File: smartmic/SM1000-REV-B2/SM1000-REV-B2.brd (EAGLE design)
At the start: 65 x 90 mm, 176 parts, among them CN1 HDR100-3, CN10 MJ-3523-SMT, CN11 HDR100-3, CN12 DF11-16DS, CN2 MOLEX-MINI-B-SMT, CN3 RASM712PX, CN4 RJ-45, CN5 MJ-3523-SMT, CN6 MJ-3523-SMT, CN7 MJ-3523-SMT, CN8 MJ-3523-SMT, CN9 MJ-3523-SMT, J1 JMP-2PIN, J2 JMP-2PIN, J3 JMP-2PIN, J4 JMP-2PIN, J5 JMP-2PIN, J7 JMP-2PIN, P1 TPAD50, P10 TPAD50, P11 TPAD50, P12 TPAD50, P13 TPAD50, P14 TPAD50, P15 TPAD50, P16 TPAD50, P17 TPAD50, P18 TPAD50, P19 TPAD50, P2 TPAD50, P20 TPAD50, P3 TPAD50, P4 TPAD50, P5 TPAD50, P6 TPAD50, P7 TPAD50, P8 TPAD50, P9 TPAD50, SW1 SW-BOURNS-7914S, SW2 SW-BOURNS-7914S, SW3 DPDT, SW4 SW-BOURNS-7914S, T1 SM-LP-5001, T2 SM-LP-5001, U1 STM32F405, U2 LD3985M33R, U3 STMPS2141, U4 EMIF02-USB03F2, U5 TPS54329E, U6 LMV341, U7 LMV341, U8 LM386M-1, U9 LMV341

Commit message: Updates indicated in change log - RGB
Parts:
- moved LED5 0.50 mm to (21.2, 44.0)
- moved LED8 0.50 mm to (2.50, 48.5)
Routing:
- net +3.3V: track 19.8 -> 20.8 mm
- net N$19: track 2.52 -> 3.27 mm
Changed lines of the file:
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@@
 <layer number="17" name="Pads" color="2" fill="1" visible="yes" active="yes"/>
 <layer number="18" name="Vias" color="2" fill="1" visible="yes" active="yes"/>
-<layer number="19" name="Unrouted" color="6" fill="1" visible="no" active="yes"/>
+<layer number="19" name="Unrouted" color="6" fill="1" visible="yes" active="yes"/>
 <layer number="20" name="Dimension" color="15" fill="1" visible="yes" active="yes"/>
-<layer number="21" name="tPlace" color="7" fill="1" visible="no" active="yes"/>
+<layer number="21" name="tPlace" color="7" fill="1" visible="yes" active="yes"/>
 <layer number="22" name="bPlace" color="7" fill="1" visible="no" active="yes"/>
 <layer number="23" name="tOrigins" color="15" fill="1" visible="yes" active="yes"/>
 <layer number="24" name="bOrigins" color="15" fill="1" visible="no" active="yes"/>
-<layer number="25" name="tNames" color="7" fill="1" visible="no" active="yes"/>
+<layer number="25" name="tNames" color="7" fill="1" visible="yes" active="yes"/>
 <layer number="26" name="bNames" color="7" fill="1" visible="no" active="yes"/>
 <layer number="27" name="tValues" color="7" fill="1" visible="no" active="yes"/>
@@
 <layer number="200" name="200bmp" color="1" fill="10" visible="no" active="no"/>
 <layer number="201" name="Construction" color="7" fill="1" visible="no" active="yes"/>
-<layer number="202" name="TDIM" color="7" fill="1" visible="yes" active="yes"/>
+<layer number="202" name="TDIM" color="7" fill="1" visible="no" active="yes"/>
 <layer number="203" name="BDIM" color="7" fill="1" visible="no" active="yes"/>
 <layer number="204" name="BRD-DIM" color="7" fill="1" visible="no" active="yes"/>
@@
 <attribute name="VALUE" x="5.4625" y="49.25" size="1" layer="27" font="vector" ratio="10" rot="R270"/>
 </element>
-<element name="LED5" library="_Coherix" package="LED-LTST" value="LED-RED,V" x="21.25" y="44.5" locked="yes" smashed="yes" rot="R270">
-<attribute name="NAME" x="21.8" y="42.05" size="0.8128" layer="25"/>
+<element name="LED5" library="_Coherix" package="LED-LTST" value="LED-RED,V" x="21.25" y="44" locked="yes" smashed="yes" rot="R270">
+<attribute name="NAME" x="22.2" y="42.05" size="0.8128" layer="25"/>
 </element>
 <element name="R17" library="AA-ipc-7351-resistor" package="RESC1608X55N" value="1K,1%" x="18.75" y="44.5" locked="yes" smashed="yes" rot="R90">
@@
 <attribute name="NAME" x="4" y="49.7" size="0.8128" layer="25"/>
 </element>
-<element name="LED8" library="_Coherix" package="LED-LTST" value="LED-RED,RA" x="2.5" y="48" locked="yes" smashed="yes" rot="R270">
-<attribute name="NAME" x="1.2" y="45.5" size="0.8128" layer="25"/>
+<element name="LED8" library="_Coherix" package="LED-LTST" value="LED-RED,RA" x="2.5" y="48.5" locked="yes" smashed="yes" rot="R270">
+<attribute name="NAME" x="0.8" y="45.4" size="0.8128" layer="25"/>
 </element>
 <element name="CN9" library="_RoweTel" package="MJ-3523-SMT" value="MJ-3523-SMT" x="43" y="8" locked="yes" smashed="yes" rot="MR270">
@@
 <wire x1="18.75" y1="46.95" x2="21.25" y2="46.95" width="0.4" layer="1"/>
 <polygon width="0.2" layer="1" isolate="0.3">
-<vertex x="3.5" y="50"/>
-<vertex x="1" y="50"/>
+<vertex x="3.5" y="51"/>
+<vertex x="1" y="51"/>
 <vertex x="1" y="46"/>
 <vertex x="6.5" y="46"/>
@@
 <wire x1="23.75" y1="48.55" x2="21.25" y2="48.55" width="0.4" layer="1"/>
 <wire x1="18.75" y1="48.55" x2="21.25" y2="48.55" width="0.4" layer="1"/>
-<wire x1="18.75" y1="45.3" x2="19.7" y2="45.3" width="0.2" layer="1"/>
-<wire x1="19.7" y1="45.3" x2="20.5" y2="44.5" width="0.2" layer="1"/>
-<wire x1="20.5" y1="44.5" x2="22" y2="44.5" width="0.2" layer="1"/>
-<wire x1="22" y1="44.5" x2="22.5" y2="45" width="0.2" layer="1"/>
+<wire x1="18.75" y1="45.3" x2="19.2" y2="45.3" width="0.2" layer="1"/>
 <wire x1="22.5" y1="45" x2="22.5" y2="47" width="0.2" layer="1"/>
 <wire x1="22.5" y1="47" x2="23.02" y2="47.52" width="0.2" layer="1"/>
@@
 <wire x1="15" y1="46.5" x2="17.05" y2="48.55" width="0.4" layer="1"/>
 <wire x1="17.05" y1="48.55" x2="18.75" y2="48.55" width="0.4" layer="1"/>
+<wire x1="19.2" y1="45.3" x2="19.5" y2="45.3" width="0.2" layer="1"/>
+<wire x1="19.5" y1="45.3" x2="19.7" y2="45.3" width="0.2" layer="1"/>
+<wire x1="19.7" y1="45.3" x2="20" y2="45" width="0.2" layer="1"/>
+<wire x1="20" y1="45" x2="20" y2="44.5" width="0.2" layer="1"/>
+<wire x1="20" y1="44.5" x2="20.5" y2="44" width="0.2" layer="1"/>
+<wire x1="20.5" y1="44" x2="22" y2="44" width="0.2" layer="1"/>
+<wire x1="22" y1="44" x2="22.5" y2="44.5" width="0.2" layer="1"/>
+<wire x1="22.5" y1="44.5" x2="22.5" y2="45" width="0.2" layer="1"/>
 </signal>
 <signal name="+5V">
@@
 <contactref element="LED5" pad="A"/>
 <contactref element="R17" pad="1"/>
-<wire x1="18.75" y1="43.7" x2="21.2" y2="43.7" width="0.4" layer="1"/>
-<wire x1="21.2" y1="43.7" x2="21.25" y2="43.75" width="0.4" layer="1"/>
+<wire x1="18.75" y1="43.7" x2="18.75" y2="43.05" width="0.2" layer="1"/>
+<wire x1="18.75" y1="43.05" x2="19" y2="42.8" width="0.2" layer="1"/>
+<wire x1="19" y1="42.8" x2="19.05" y2="42.75" width="0.2" layer="1"/>
+<wire x1="19.05" y1="42.75" x2="21.25" y2="42.75" width="0.2" layer="1"/>
 </signal>
 <signal name="N$16">

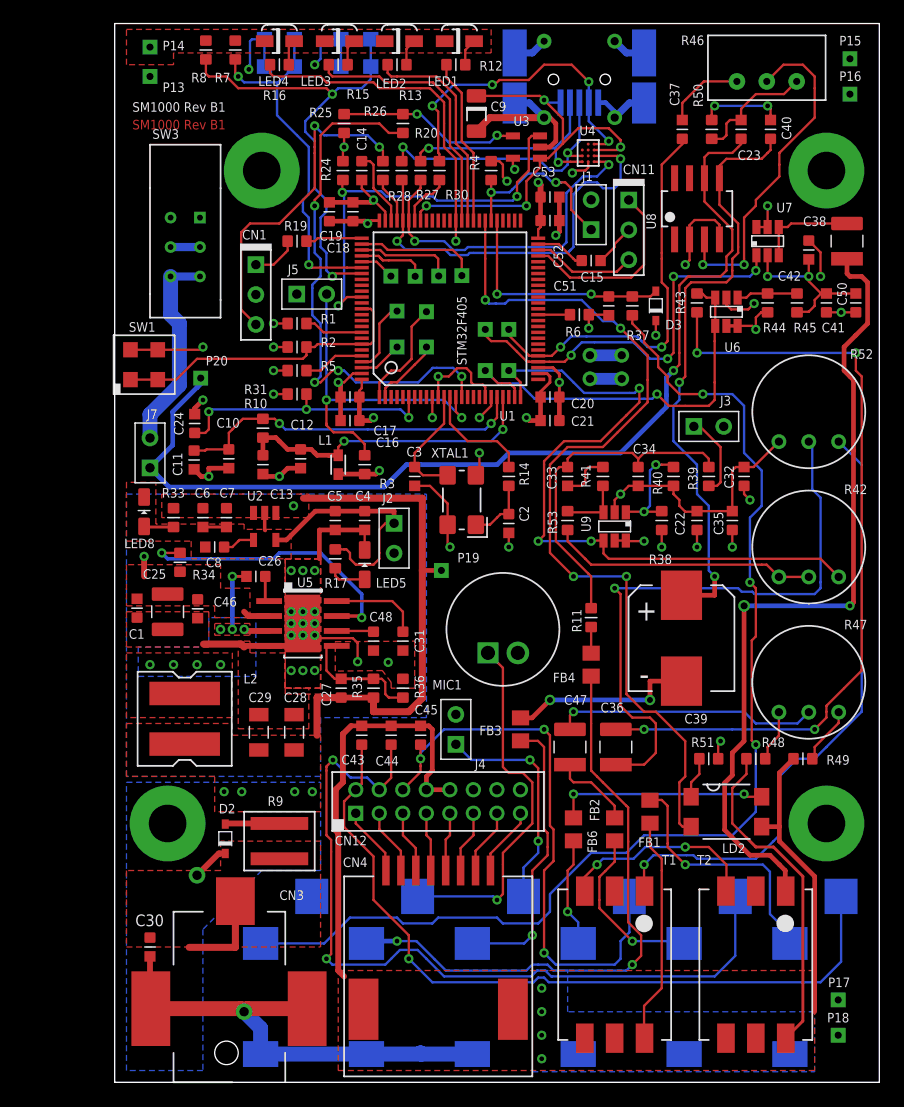
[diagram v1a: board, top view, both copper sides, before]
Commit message: 
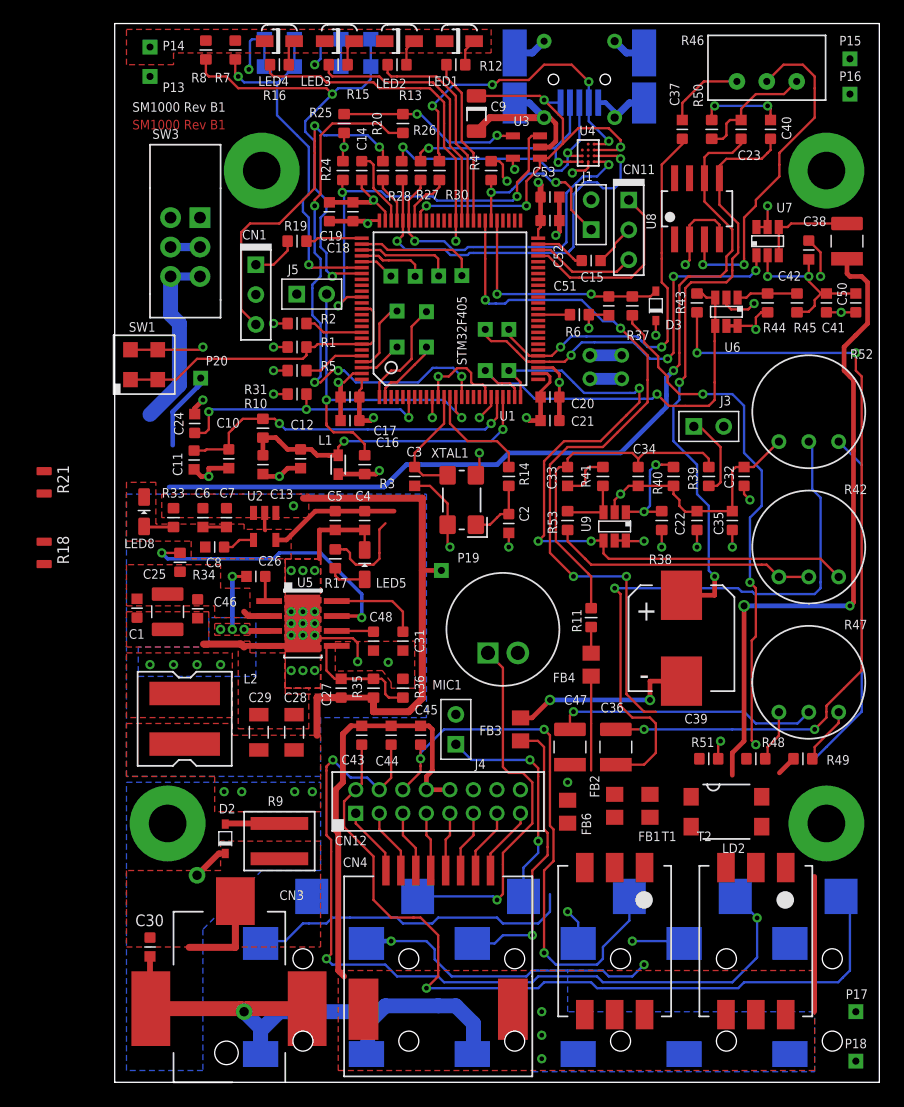
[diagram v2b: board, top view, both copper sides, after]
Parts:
- removed J2, J7: JMP-2PIN, _Coherix:JMPR-2PIN
- removed SH2, SH6: SHUNT,0.1IN, _Coherix:NOPACKAGE
- added R18, R21: 0 Ohm, _RoweTel:RR0805
- moved P18 2.66 mm to (63.0, 1.80)
- moved FB2 2.00 mm to (42.5, 23.5)
- moved T1 2.00 mm to (42.5, 12.0)
- moved T2 2.00 mm to (54.5, 12.0)
- moved P17 1.80 mm to (63.0, 6.00)
- moved FB6 1.58 mm to (38.5, 23.0)
- moved FB1 0.50 mm to (45.5, 23.5)
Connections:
- net +3.3V: now also R18.1; no longer J2.1
- net +VIN: now also R21.2; no longer J7.1
- net N$70: now also R21.1; no longer J7.2
- net VDD: now also R18.2; no longer J2.2
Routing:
- net VDD: track 89.5 -> 148.4 mm
- net N$78: track 28.2 -> 0.00 mm
- net N$85: track 98.7 -> 72.7 mm
- net N$63: track 53.1 -> 29.4 mm, vias 1 -> 0
- net N$64: track 21.6 -> 0.00 mm, vias 1 -> 0
- net N$33: track 19.3 -> 0.00 mm
- net N$74: track 18.1 -> 0.00 mm, vias 2 -> 1
- net N$76: track 50.9 -> 34.3 mm
- net +VIN: track 100.8 -> 84.2 mm, vias 2 -> 1
- net N$65: track 69.2 -> 55.9 mm
- net !CPPT!: track 77.0 -> 65.2 mm
- net RF: track 61.2 -> 49.7 mm, vias 4 -> 3
- net N$72: track 14.7 -> 4.48 mm
- net N$79: track 6.98 -> 0.00 mm
- net N$73: track 9.30 -> 3.07 mm
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
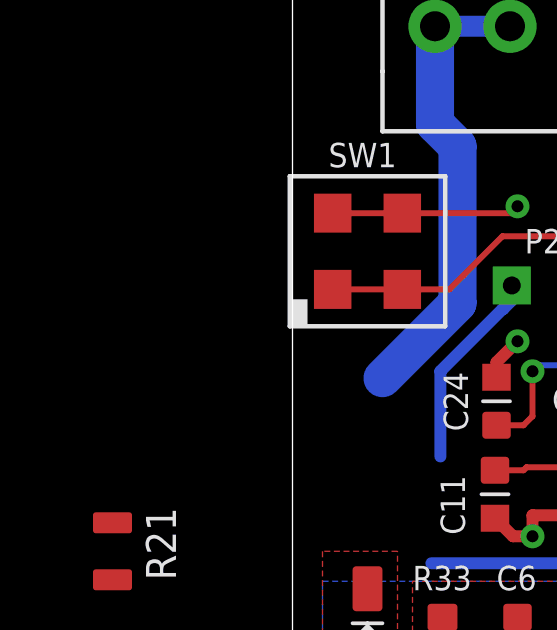
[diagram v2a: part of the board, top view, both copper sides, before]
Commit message: Items 1-5,7-12,14-20 have been implemented in schematic . Items 6 & 13 need discussion to resolve. PCB has been updated to reflect changes, but routing of changes has not been completed. Layout will be updated as time pemits. RGB - 07/17/2014
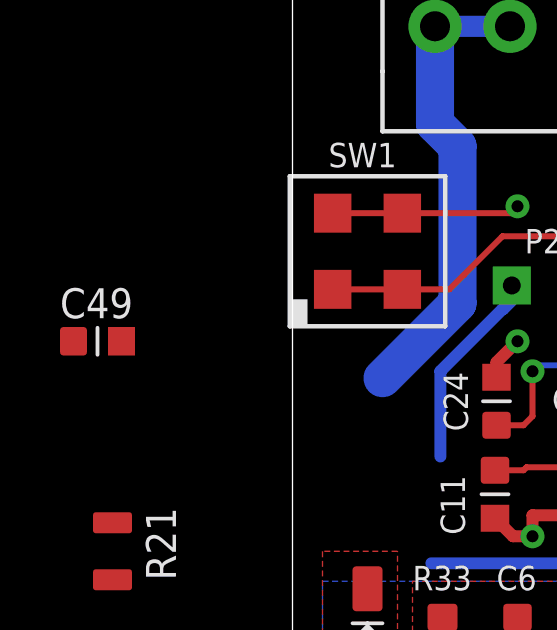
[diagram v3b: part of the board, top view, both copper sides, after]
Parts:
- added C49: 100nF,16V, AA-ipc-7351-capacitor:CAPC1608X92N
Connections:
- net GND: now also C49.2
- net NRST: now also C49.1
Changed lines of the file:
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@@
 <grid distance="0.5" unitdist="mm" unit="mm" style="dots" multiple="1" display="yes" altdistance="0.1" altunitdist="mm" altunit="mm"/>
 <layers>
-<layer number="1" name="Top" color="4" fill="1" visible="no" active="yes"/>
-<layer number="2" name="GND" color="3" fill="1" visible="no" active="yes"/>
+<layer number="1" name="Top" color="4" fill="1" visible="yes" active="yes"/>
+<layer number="2" name="GND" color="3" fill="1" visible="yes" active="yes"/>
 <layer number="3" name="Route3" color="4" fill="3" visible="no" active="no"/>
 <layer number="4" name="Route4" color="1" fill="4" visible="no" active="no"/>
@@
 <layer number="19" name="Unrouted" color="6" fill="1" visible="yes" active="yes"/>
 <layer number="20" name="Dimension" color="15" fill="1" visible="yes" active="yes"/>
-<layer number="21" name="tPlace" color="7" fill="1" visible="no" active="yes"/>
-<layer number="22" name="bPlace" color="7" fill="1" visible="yes" active="yes"/>
-<layer number="23" name="tOrigins" color="15" fill="1" visible="no" active="yes"/>
-<layer number="24" name="bOrigins" color="15" fill="1" visible="yes" active="yes"/>
-<layer number="25" name="tNames" color="7" fill="1" visible="no" active="yes"/>
-<layer number="26" name="bNames" color="7" fill="1" visible="yes" active="yes"/>
+<layer number="21" name="tPlace" color="7" fill="1" visible="yes" active="yes"/>
+<layer number="22" name="bPlace" color="7" fill="1" visible="no" active="yes"/>
+<layer number="23" name="tOrigins" color="15" fill="1" visible="yes" active="yes"/>
+<layer number="24" name="bOrigins" color="15" fill="1" visible="no" active="yes"/>
+<layer number="25" name="tNames" color="7" fill="1" visible="yes" active="yes"/>
+<layer number="26" name="bNames" color="7" fill="1" visible="no" active="yes"/>
 <layer number="27" name="tValues" color="7" fill="1" visible="no" active="yes"/>
 <layer number="28" name="bValues" color="7" fill="1" visible="no" active="yes"/>
@@
 <element name="R18" library="_RoweTel" package="RR0805" value="0 Ohm" x="-6" y="45" rot="R270"/>
 <element name="R21" library="_RoweTel" package="RR0805" value="0 Ohm" x="-6" y="51" rot="R270"/>
+<element name="C49" library="AA-ipc-7351-capacitor" package="CAPC1608X92N" value="100nF,16V" x="-6.5" y="58"/>
 </elements>
 <signals>
@@
 <wire x1="21.5" y1="5" x2="21.5" y2="2.5" width="1.27" layer="16"/>
 <wire x1="21.5" y1="2.5" x2="21.4" y2="2.4" width="1.27" layer="16"/>
-<wire x1="39.96" y1="18.25" x2="51.96" y2="18.25" width="0" layer="19" extent="1-1"/>
+<contactref element="C49" pad="2"/>
+<wire x1="57.97" y1="85.08" x2="62.5" y2="84" width="0" layer="19" extent="1-1"/>
+<wire x1="45" y1="83.25" x2="50.75" y2="80.2" width="0" layer="19" extent="1-16"/>
+<wire x1="37.5" y1="81.5" x2="41.1" y2="83.275" width="0" layer="19" extent="1-16"/>
+<wire x1="39.1" y1="77.5" x2="37" y2="79.5" width="0" layer="19" extent="1-1"/>
+<wire x1="37.8" y1="75.25" x2="38.9" y2="77.3" width="0" layer="19" extent="1-1"/>
+<wire x1="40.5" y1="75.02" x2="40" y2="77.5" width="0" layer="19" extent="1-1"/>
+<wire x1="43.7" y1="72.46" x2="40.5" y2="75.02" width="0" layer="19" extent="1-1"/>
+<wire x1="45" y1="87.5" x2="45" y2="83.25" width="0" layer="19" extent="16-16"/>
+<wire x1="34" y1="87.5" x2="34" y2="83.25" width="0" layer="19" extent="16-16"/>
+<wire x1="41.95" y1="65.25" x2="41.35" y2="69.85" width="0" layer="19" extent="1-1"/>
+<wire x1="40.4" y1="59.8" x2="40.3" y2="64.1" width="0" layer="19" extent="1-1"/>
+<wire x1="37" y1="60" x2="40.4" y2="59.8" width="0" layer="19" extent="1-1"/>
+<wire x1="32" y1="57.5" x2="35" y2="56.5" width="0" layer="19" extent="1-1"/>
+<wire x1="31" y1="53.5" x2="31" y2="56.5" width="0" layer="19" extent="1-1"/>
+<wire x1="28.3" y1="49.2" x2="30.7" y2="51.6" width="0" layer="19" extent="1-1"/>
+<wire x1="27" y1="56.5" x2="31" y2="56.5" width="0" layer="19" extent="1-1"/>
+<wire x1="33.5" y1="45.5" x2="28.5" y2="45.5" width="0" layer="19" extent="1-1"/>
+<wire x1="48.865" y1="72.865" x2="43.7" y2="72.46" width="0" layer="19" extent="1-1"/>
+<wire x1="55.5" y1="70.3" x2="51.405" y2="71.65" width="0" layer="19" extent="1-1"/>
+<wire x1="54.35" y1="66.2" x2="55.5" y2="68.5" width="0" layer="19" extent="1-1"/>
+<wire x1="21.25" y1="46.95" x2="25.5" y2="50.7" width="0" layer="19" extent="1-1"/>
+<wire x1="17" y1="43.5" x2="17.4" y2="44.5" width="0" layer="19" extent="1-1"/>
+<wire x1="16" y1="43.5" x2="17" y2="43.5" width="0" layer="19" extent="1-1"/>
+<wire x1="15" y1="43.5" x2="16" y2="43.5" width="0" layer="19" extent="1-1"/>
+<wire x1="17" y1="40" x2="17" y2="43.5" width="0" layer="19" extent="1-1"/>
+<wire x1="17" y1="39" x2="17" y2="40" width="0" layer="19" extent="1-1"/>
+<wire x1="16" y1="40" x2="17" y2="40" width="0" layer="19" extent="1-1"/>
+<wire x1="17" y1="38" x2="17" y2="39" width="0" layer="19" extent="1-1"/>
+<wire x1="17.25" y1="37.75" x2="17" y2="38" width="0" layer="19" extent="1-1"/>
+<wire x1="15" y1="40" x2="16" y2="40" width="0" layer="19" extent="1-1"/>
+<wire x1="15" y1="39" x2="15" y2="40" width="0" layer="19" extent="1-1"/>
+<wire x1="15" y1="38" x2="15" y2="39" width="0" layer="19" extent="1-1"/>
+<wire x1="16" y1="39" x2="17" y2="39" width="0" layer="19" extent="1-1"/>
+<wire x1="22" y1="36.7" x2="20.65" y2="37.35" width="0" layer="19" extent="1-1"/>
+<wire x1="23.25" y1="35.7" x2="22" y2="36.7" width="0" layer="19" extent="1-1"/>
+<wire x1="24.5" y1="36.7" x2="23.25" y2="35.7" width="0" layer="19" extent="1-1"/>
+<wire x1="24.5" y1="34.3" x2="23.25" y2="35.7" width="0" layer="19" extent="1-1"/>
+<wire x1="16" y1="35" x2="16" y2="37.095" width="0" layer="19" extent="1-1"/>
+<wire x1="17" y1="35" x2="16" y2="35" width="0" layer="19" extent="1-1"/>
+<wire x1="15" y1="35" x2="16" y2="35" width="0" layer="19" extent="1-1"/>
+<wire x1="7.05" y1="39.45" x2="7.55" y2="37.25" width="0" layer="19" extent="1-1"/>
+<wire x1="4.5" y1="38.5" x2="7.05" y2="39.45" width="0" layer="19" extent="1-1"/>
+<wire x1="1.9" y1="39.5" x2="4.5" y2="38.5" width="0" layer="19" extent="1-1"/>
+<wire x1="15.25" y1="31.25" x2="15" y2="35" width="0" layer="19" extent="1-1"/>
+<wire x1="12.25" y1="31.25" x2="15.25" y2="31.25" width="0" layer="19" extent="1-1"/>
+<wire x1="12.8" y1="46.9" x2="15" y2="43.5" width="0" layer="19" extent="1-1"/>
+<wire x1="12.8" y1="51.5" x2="12.75" y2="48.4" width="0" layer="19" extent="1-1"/>
+<wire x1="9.7" y1="52.2" x2="12.6" y2="51.7" width="0" layer="19" extent="1-1"/>
+<wire x1="9.5" y1="47.2" x2="12.75" y2="46.95" width="0" layer="19" extent="1-1"/>
+<wire x1="7.7" y1="45.5" x2="7.5" y2="47.2" width="0" layer="19" extent="1-1"/>
+<wire x1="6.8" y1="56.8" x2="6.75" y2="52.1" width="0" layer="19" extent="1-1"/>
+<wire x1="2.5" y1="49.75" x2="6.75" y2="52.1" width="0" layer="19" extent="1-1"/>
+<wire x1="19.2" y1="56.25" x2="15.8" y2="52.2" width="0" layer="19" extent="1-1"/>
+<wire x1="14.7" y1="62.5" x2="19" y2="59.5" width="0" layer="19" extent="1-1"/>
+<wire x1="15.48" y1="67" x2="14.7" y2="62.5" width="0" layer="19" extent="1-1"/>
+<wire x1="12" y1="66.96" x2="15.48" y2="67" width="0" layer="19" extent="1-1"/>
+<wire x1="29" y1="31.27" x2="24.5" y2="34.3" width="0" layer="19" extent="1-1"/>
+<wire x1="28.05" y1="88.5" x2="34" y2="87.5" width="0" layer="19" extent="1-16"/>
+<wire x1="22.95" y1="88.5" x2="27.95" y2="88.5" width="0" layer="19" extent="1-1"/>
+<wire x1="17.85" y1="88.5" x2="22.95" y2="88.5" width="0" layer="19" extent="1-1"/>
+<wire x1="12.75" y1="88.5" x2="17.85" y2="88.5" width="0" layer="19" extent="1-1"/>
+<wire x1="10.25" y1="88.55" x2="12.75" y2="88.5" width="0" layer="19" extent="1-1"/>
+<wire x1="7.75" y1="88.55" x2="10.25" y2="88.55" width="0" layer="19" extent="1-1"/>
+<wire x1="3" y1="88" x2="7.75" y2="88.55" width="0" layer="19" extent="1-1"/>
+<wire x1="34.27" y1="36.5" x2="29" y2="31.27" width="0" layer="19" extent="1-1"/>
+<wire x1="18.25" y1="74.8" x2="15.48" y2="67" width="0" layer="19" extent="1-1"/>
+<wire x1="43.7" y1="50.7" x2="43.1" y2="59.8" width="0" layer="19" extent="1-1"/>
+<wire x1="39.96" y1="18.25" x2="29" y2="31.27" width="0" layer="19" extent="1-1"/>
+<wire x1="51.96" y1="18.25" x2="39.96" y2="18.25" width="0" layer="19" extent="1-1"/>
 <wire x1="63.5" y1="10.5" x2="51.96" y2="18.25" width="0" layer="19" extent="1-2"/>
+<wire x1="29" y1="6.5" x2="39.96" y2="18.25" width="0" layer="19" extent="1-16"/>
+<wire x1="-5.7" y1="58" x2="3.07" y2="6.26" width="0" layer="19" extent="1-1"/>
 </signal>
 <signal name="SCL">
@@
 <wire x1="20.25" y1="55.25" x2="21.25" y2="54.25" width="0.2" layer="1"/>
 <wire x1="29.5" y1="56.5" x2="29" y2="57" width="0.2" layer="1"/>
+<contactref element="C49" pad="1"/>
+<wire x1="-7.3" y1="58" x2="21.25" y2="53.3" width="0" layer="19" extent="1-1"/>
 </signal>
 <signal name="BOOT0">
